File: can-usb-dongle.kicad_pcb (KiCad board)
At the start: 2 copper layers, 41 parts, among them SW1 SW_PUSH, U1 STM32F302C8T, U2 SN65HVD256, U3 NUF2042XV6, U4 MCP1700, U5 SiP32431, X1 16MHz 10ppm

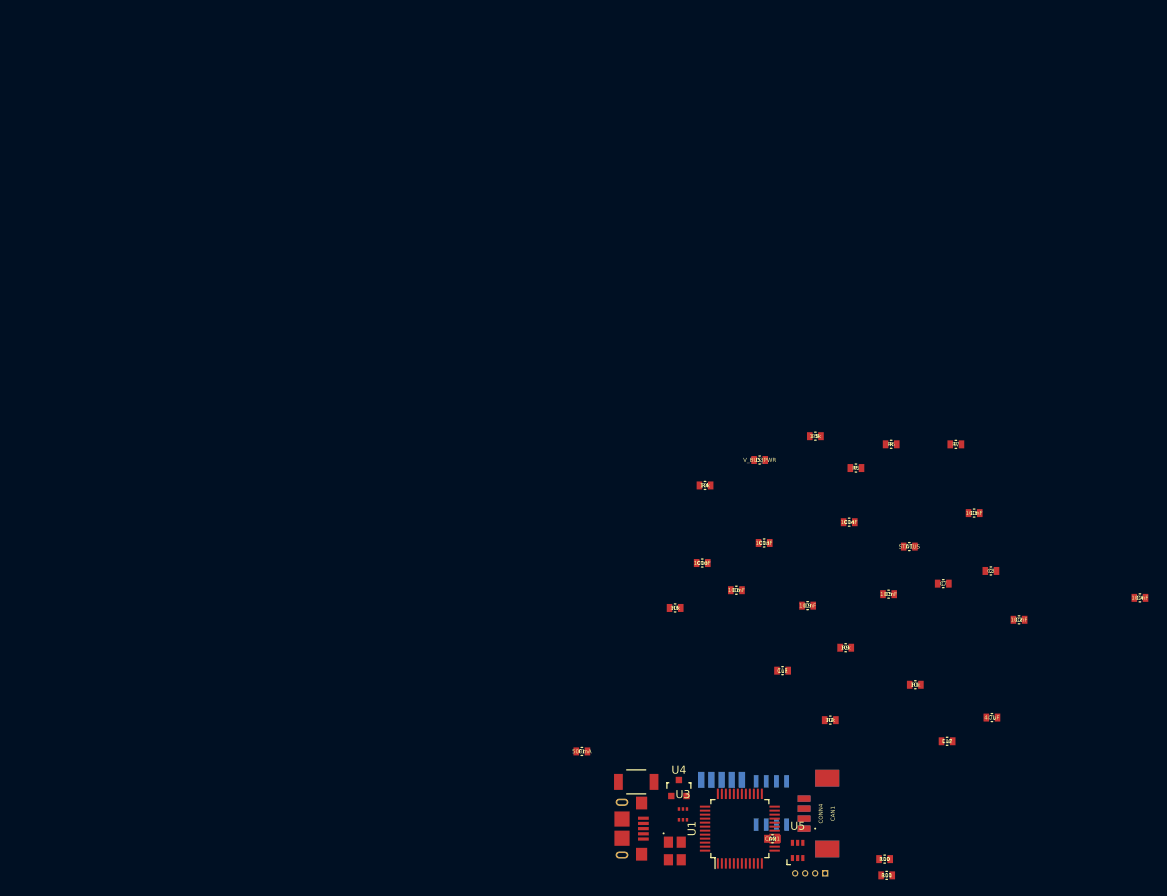
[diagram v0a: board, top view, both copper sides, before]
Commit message: Most components placed.
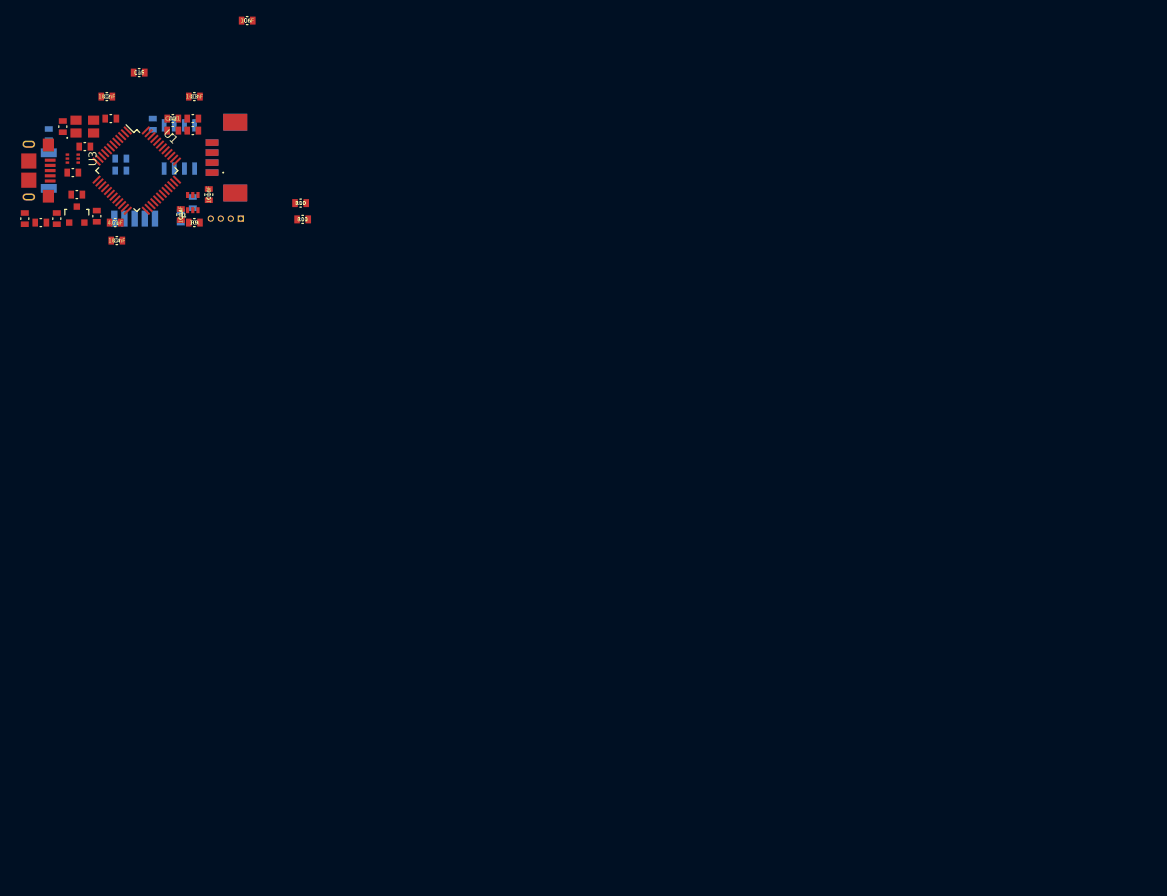
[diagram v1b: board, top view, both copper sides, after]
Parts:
- added C15: 1uF, _std:_0603, F.Cu at (60.3, 32.8)
- C5, C9, R1, R2, R3, R4, SW1: moved to B.Cu
- C6: value 100nF -> 10nF
- C7, C8: value C -> 10pF
- moved C4 135.5 mm to (57.5, 53.8), turned to 180 degrees
- moved C2 131.5 mm to (56.2, 35.8)
- moved C1 125.8 mm to (57.3, 51.5), turned to 180 degrees
- moved C12 124.9 mm to (55.0, 50.7), turned to 90 degrees
- moved C7 124.0 mm to (50.8, 39.5), turned to 270 degrees
- moved C8 123.7 mm to (56.8, 38.5), turned to 180 degrees
- moved R2 122.1 mm to (49.0, 40.5), turned to 90 degrees
- moved R1 118.3 mm to (58.0, 45.0)
- moved D1 117.9 mm to (46.0, 51.0), turned to 90 degrees
- moved D2 117.1 mm to (64.5, 38.5), turned to 180 degrees
- moved X1 116.8 mm to (53.5, 39.5), turned to 0 degrees
- moved U3 112.0 mm to (52.0, 43.5), turned to 90 degrees
- moved U1 111.6 mm to (60.0, 45.0), turned to 315 degrees
- moved U5 110.8 mm to (67.0, 49.0)
- moved CONN3 110.7 mm to (46.5, 45.0)
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
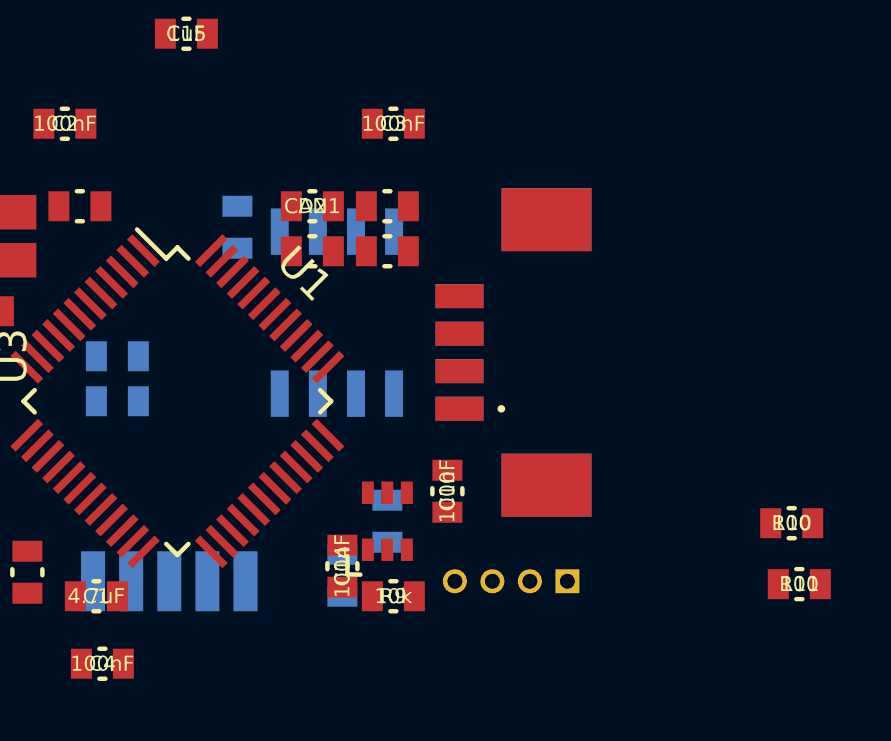
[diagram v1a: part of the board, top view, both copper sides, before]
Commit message: Connect CAN bus power LED to GPIO, update connector footprints.
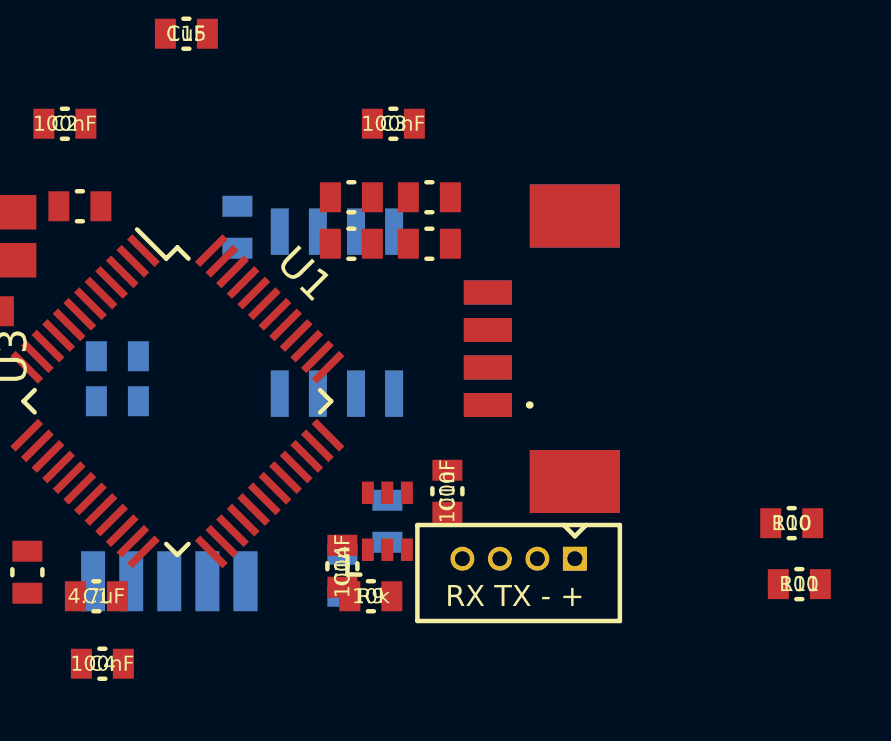
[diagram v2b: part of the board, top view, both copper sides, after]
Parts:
- moved D3 1.43 mm to (68.4, 38.2)
- moved R7 1.42 mm to (68.4, 39.8)
- moved D2 1.33 mm to (65.8, 38.2)
- moved R6 1.32 mm to (65.8, 39.8)
- moved CONN4 0.95 mm to (73.2, 43.2)
- moved CONN5 0.95 mm to (73.2, 43.2)
- moved CONN1 0.79 mm to (73.2, 50.2)
- moved R9 0.75 mm to (66.5, 51.5)
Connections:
- net /CAN1_LED renamed /CAN1_STATUS_LED
- D3 pad 2: /V_BUS -> /CAN1_PWR_LED
- U1 pad 12: Net-(U1-Pad12) -> (no net)
- U1 pad 13: Net-(U1-Pad13) -> (no net)
- U1 pad 14: Net-(U1-Pad14) -> (no net)
- U1 pad 15: Net-(U1-Pad15) -> (no net)
- U1 pad 16: Net-(U1-Pad16) -> (no net)
- U1 pad 17: Net-(U1-Pad17) -> (no net)
- U1 pad 2: Net-(U1-Pad2) -> (no net)
- U1 pad 20: /V_BUS_ENABLE -> /CAN1_PWR_LED
- U1 pad 22: Net-(U1-Pad22) -> (no net)
- U1 pad 25: Net-(U1-Pad25) -> (no net)
- U1 pad 26: Net-(U1-Pad26) -> (no net)
- U1 pad 27: Net-(U1-Pad27) -> (no net)
- U1 pad 28: Net-(U1-Pad28) -> (no net)
- U1 pad 29: Net-(U1-Pad29) -> (no net)
- U1 pad 3: Net-(U1-Pad3) -> (no net)
- U1 pad 30: Net-(U1-Pad30) -> (no net)
- U1 pad 31: Net-(U1-Pad31) -> (no net)
- U1 pad 38: Net-(U1-Pad38) -> (no net)
- U1 pad 39: Net-(U1-Pad39) -> /V_BUS_ENABLE
- U1 pad 4: Net-(U1-Pad4) -> (no net)
- U1 pad 40: Net-(U1-Pad40) -> (no net)
- U1 pad 41: Net-(U1-Pad41) -> (no net)
- U5 pad 6: Net-(U5-Pad6) -> (no net)
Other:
- board text added: "+ - TX RX"
- board text added: "RX TX - +"

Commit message: Change DRC minimal dimmensions
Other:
- net class Default: trace_width 0.25 -> 0.2; via_dia 0.6 -> 0.8
- net class limit added: clearance 0.1524, trace_width 0.1524, via_dia 0.7, via_drill 0.3
- rule trace_min: 0.2 -> 0.1524
- rule via_min_size: 0.4 -> 0.7
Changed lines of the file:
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@@
     (links 115)
     (no_connects 115)
-    (area 0 0 0 0)
+    (area 25.087299 25.474999 91.421702 60.2)
     (thickness 1.6)
     (drawings 8)
@@
   )
   (setup
-    (last_trace_width 0.25)
+    (last_trace_width 0.2)
+    (user_trace_width 0.1524)
+    (user_trace_width 0.16)
+    (user_trace_width 0.2)
+    (user_trace_width 0.25)
     (trace_clearance 0.2)
     (zone_clearance 0.508)
     (zone_45_only no)
-    (trace_min 0.2)
+    (trace_min 0.1524)
     (segment_width 0.2)
     (edge_width 0.1)
-    (via_size 0.6)
+    (via_size 0.8)
     (via_drill 0.4)
-    (via_min_size 0.4)
+    (via_min_size 0.7)
     (via_min_drill 0.3)
+    (user_via 0.7 0.3)
+    (user_via 0.8 0.4)
+    (user_via 0.9 0.4)
+    (user_via 1 0.5)
     (uvia_size 0.3)
     (uvia_drill 0.1)
@@
   (net_class Default "This is the default net class."
     (clearance 0.2)
-    (trace_width 0.25)
-    (via_dia 0.6)
+    (trace_width 0.2)
+    (via_dia 0.8)
     (via_drill 0.4)
     (uvia_dia 0.3)
@@
     (add_net VCC)
   )
+  (net_class limit ""
+    (clearance 0.1524)
+    (trace_width 0.1524)
+    (via_dia 0.7)
+    (via_drill 0.3)
+    (uvia_dia 0.3)
+    (uvia_drill 0.1)
+  )
   (module _connectors:_Molex-PicoBlade-SMD-4 (layer F.Cu)

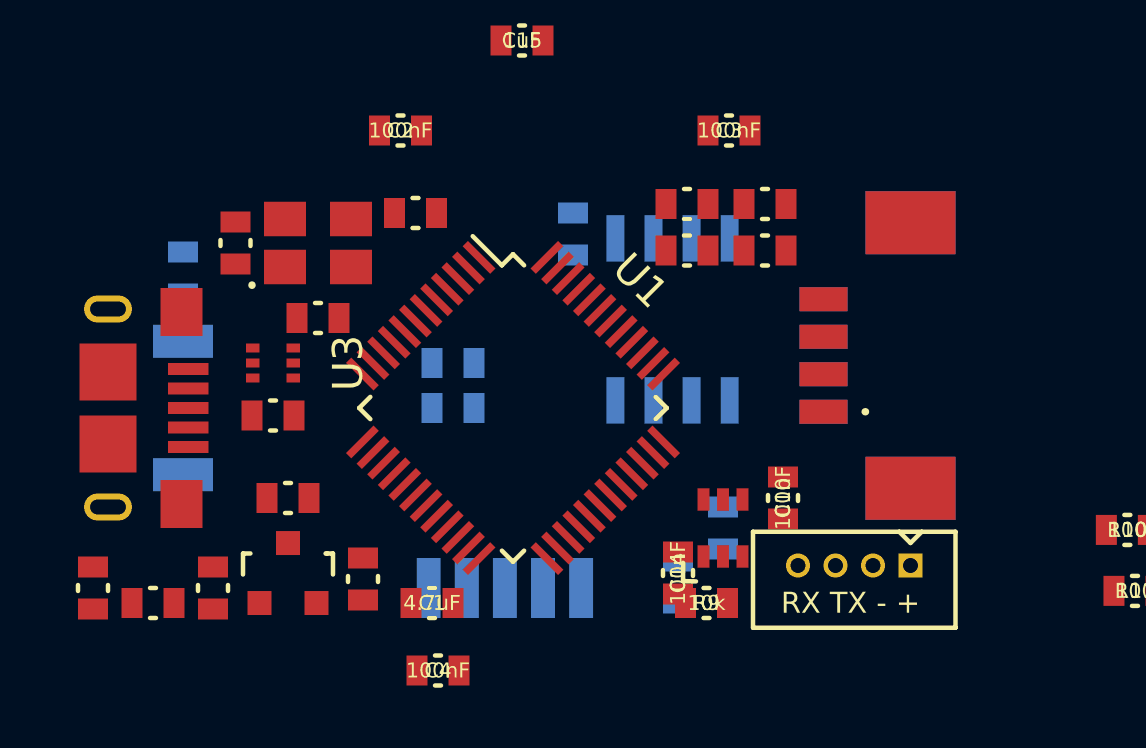
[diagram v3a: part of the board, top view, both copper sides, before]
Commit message: PCB layer setting, correct edge cut layer
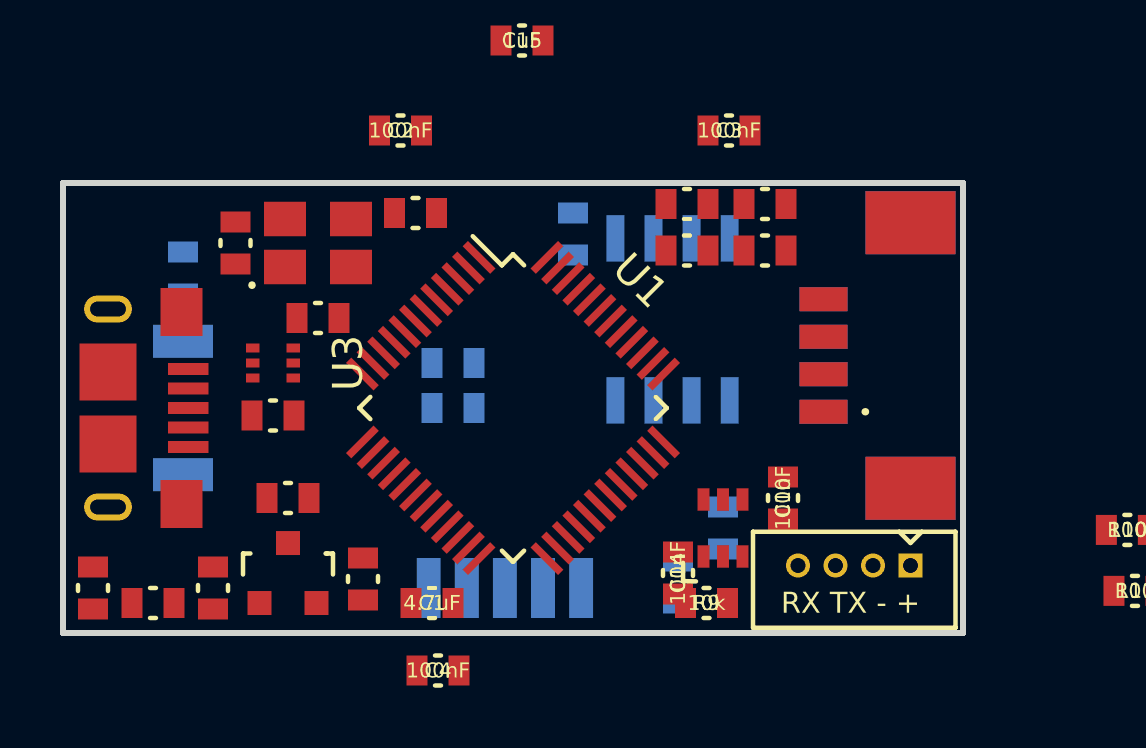
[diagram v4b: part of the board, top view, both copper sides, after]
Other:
- board outline added: 30 x 15 mm
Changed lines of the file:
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@@
     (0 F.Cu signal)
     (31 B.Cu signal)
-    (32 B.Adhes user)
-    (33 F.Adhes user)
     (34 B.Paste user)
     (35 F.Paste user)
@@
     (38 B.Mask user)
     (39 F.Mask user)
-    (40 Dwgs.User user)
     (41 Cmts.User user)
-    (42 Eco1.User user)
-    (43 Eco2.User user)
     (44 Edge.Cuts user)
-    (45 Margin user)
-    (46 B.CrtYd user)
-    (47 F.CrtYd user)
-    (48 B.Fab user)
-    (49 F.Fab user)
   )
   (setup
@@
     (trace_min 0.1524)
     (segment_width 0.2)
-    (edge_width 0.1)
+    (edge_width 0.2)
     (via_size 0.8)
     (via_drill 0.4)
@@
     (arrow2b (pts (xy 45 57.499999) (xy 46.126504 56.913578)))
   )
-  (gr_line (start 75 37.5) (end 45 37.5) (layer Dwgs.User) (width 0.2))
-  (gr_line (start 75 52.5) (end 75 37.5) (layer Dwgs.User) (width 0.2))
-  (gr_line (start 45 52.5) (end 75 52.5) (layer Dwgs.User) (width 0.2))
-  (gr_line (start 45 37.5) (end 45 52.5) (layer Dwgs.User) (width 0.2))
+  (gr_line (start 75 37.5) (end 45 37.5) (layer Edge.Cuts) (width 0.2))
+  (gr_line (start 75 52.5) (end 75 37.5) (layer Edge.Cuts) (width 0.2))
+  (gr_line (start 45 52.5) (end 75 52.5) (layer Edge.Cuts) (width 0.2))
+  (gr_line (start 45 37.5) (end 45 52.5) (layer Edge.Cuts) (width 0.2))
   (segment (start 28.3079 28.8202) (end 28.1174 29.0107) (width 0.25) (layer Dwgs.User) (net 0))
   (segment (start 25.4123 31.7158) (end 28.3079 28.8202) (width 0.25) (layer Dwgs.User) (net 0))

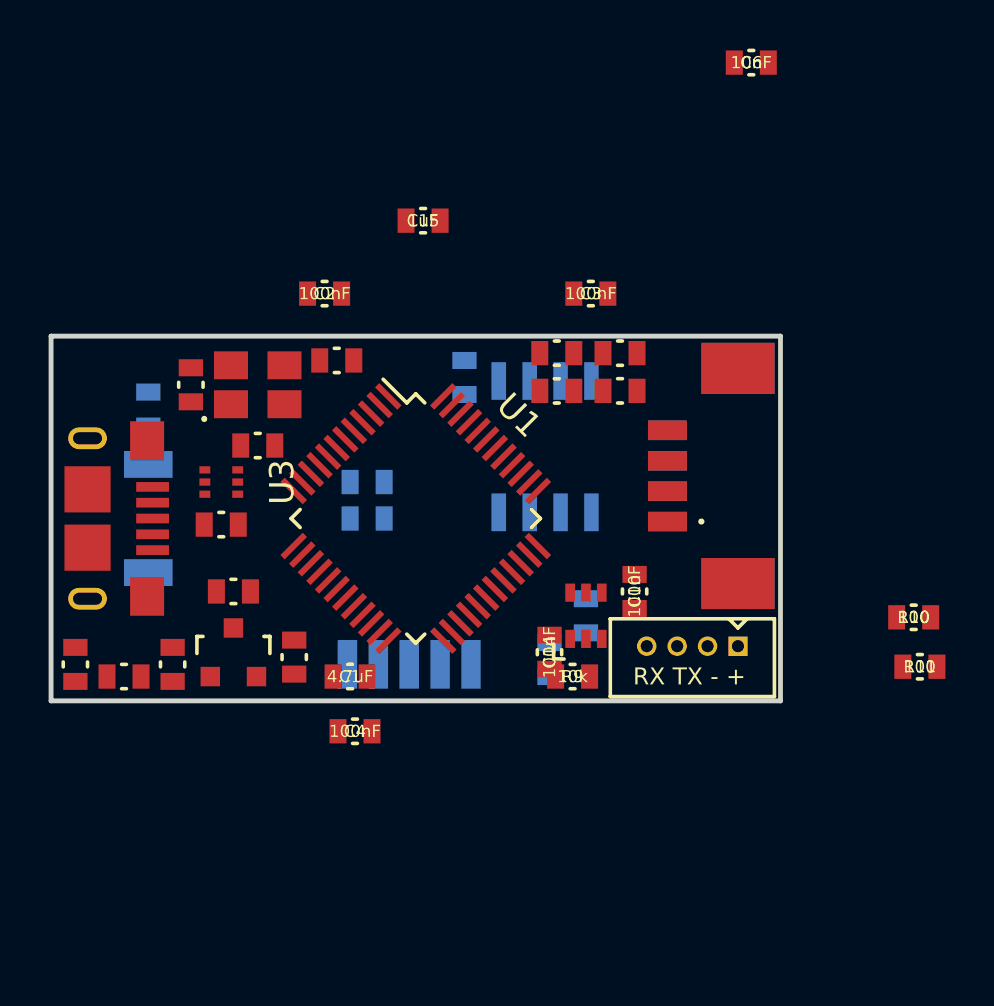
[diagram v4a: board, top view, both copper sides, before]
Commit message: Change pinout to optimize routing.
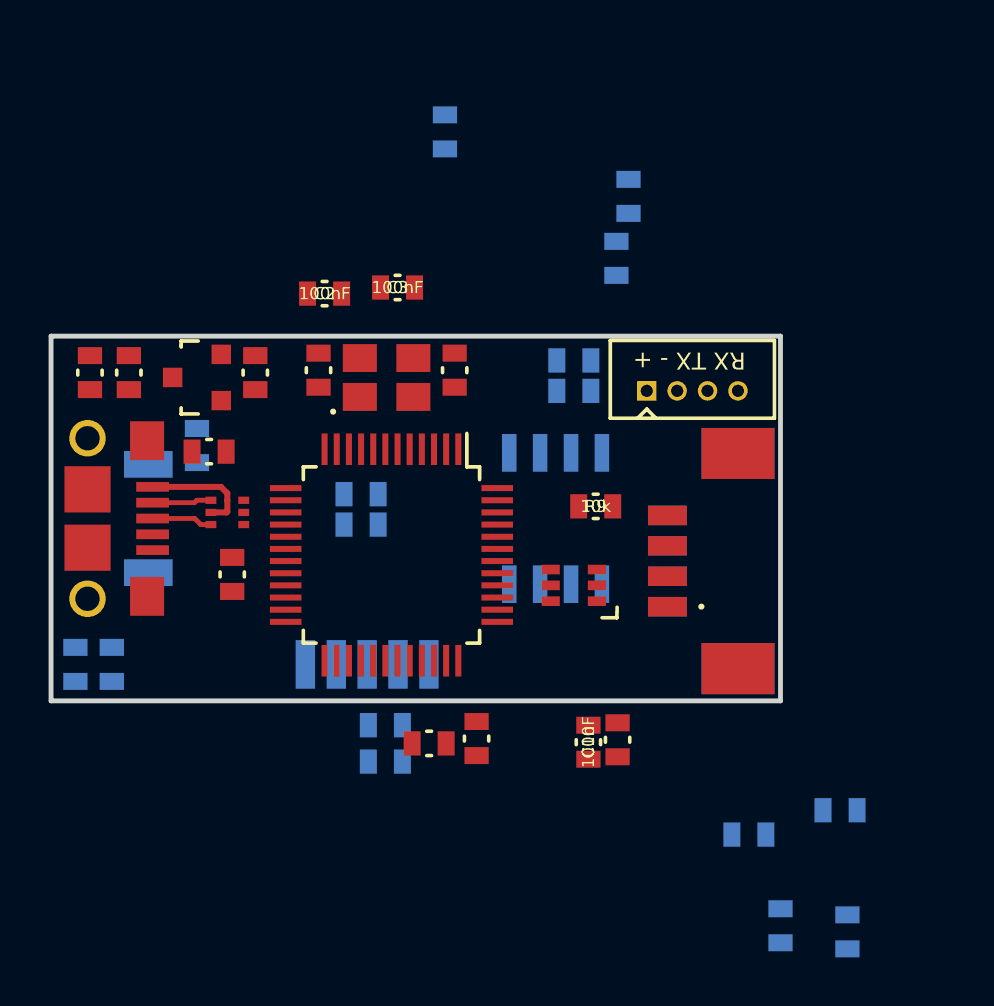
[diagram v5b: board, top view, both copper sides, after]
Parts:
- C15, C6, D1, D2, D3, R10, R11, R5, R6, R7: moved to B.Cu
- CONN3: footprint _connectors:_Micro-USB-AB-receptacle-SMT-th -> _connectors:_Micro-USB-AB-receptacle-SMT-th-no-slot
- moved D2 26.6 mm to (77.8, 62.0), turned to 270 degrees
- moved D3 24.5 mm to (75.0, 61.8), turned to 270 degrees
- moved C6 23.9 mm to (57.8, 44.0)
- moved R6 20.8 mm to (77.5, 57.0), turned to 0 degrees
- moved R7 19.0 mm to (73.7, 58.0)
- moved R11 18.2 mm to (66.5, 39.8), turned to 180 degrees
- moved R10 17.5 mm to (66.5, 38.5), turned to 180 degrees
- moved R3 17.3 mm to (68.8, 31.8)
- moved R4 16.7 mm to (68.2, 34.3)
- moved C15 12.8 mm to (57.8, 45.2)
- moved C11 12.5 mm to (46.6, 39.0)
- moved C12 11.8 mm to (53.4, 39.0), turned to 270 degrees
- moved U4 11.4 mm to (51.0, 39.2), turned to 90 degrees
- moved CONN1 11.1 mm to (69.5, 39.8), turned to 0 degrees
- moved C9 10.1 mm to (61.2, 29.1)
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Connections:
- D1 pad 1: Net-(D1-Pad1) -> GND
- D1 pad 2: /STATUS_LED -> Net-(D1-Pad2)
- D2 pad 1: Net-(D2-Pad1) -> GND
- D2 pad 2: /CAN1_STATUS_LED -> Net-(D2-Pad2)
- D3 pad 1: Net-(D3-Pad1) -> GND
- D3 pad 2: /CAN1_PWR_LED -> Net-(D3-Pad2)
- R5 pad 1: Net-(D1-Pad1) -> /STATUS_LED
- R5 pad 2: GND -> Net-(D1-Pad2)
- R6 pad 1: Net-(D2-Pad1) -> /CAN1_STATUS_LED
- R6 pad 2: GND -> Net-(D2-Pad2)
- R7 pad 1: Net-(D3-Pad1) -> /CAN1_PWR_LED
- R7 pad 2: GND -> Net-(D3-Pad2)
- U1 pad 12: (no net) -> Net-(U1-Pad12)
- U1 pad 13: (no net) -> Net-(U1-Pad13)
- U1 pad 14: (no net) -> Net-(U1-Pad14)
- U1 pad 15: (no net) -> Net-(U1-Pad15)
- U1 pad 16: (no net) -> Net-(U1-Pad16)
- U1 pad 17: (no net) -> Net-(U1-Pad17)
- U1 pad 18: /STATUS_LED -> Net-(U1-Pad18)
- U1 pad 19: /CAN1_STATUS_LED -> Net-(U1-Pad19)
- U1 pad 2: (no net) -> /CAN1_STATUS_LED
- U1 pad 20: /CAN1_PWR_LED -> Net-(U1-Pad20)
- U1 pad 21: /CAN_SILENT -> Net-(U1-Pad21)
- U1 pad 22: (no net) -> Net-(U1-Pad22)
- U1 pad 25: (no net) -> /STATUS_LED
- U1 pad 26: (no net) -> Net-(U1-Pad26)
- U1 pad 27: (no net) -> Net-(U1-Pad27)
- U1 pad 28: (no net) -> Net-(U1-Pad28)
- U1 pad 29: (no net) -> Net-(U1-Pad29)
- U1 pad 3: (no net) -> /CAN1_PWR_LED
- U1 pad 30: (no net) -> Net-(U1-Pad30)
- U1 pad 31: (no net) -> Net-(U1-Pad31)
- U1 pad 38: (no net) -> /V_BUS_ENABLE
- U1 pad 39: /V_BUS_ENABLE -> /CAN_SILENT
- U1 pad 4: (no net) -> Net-(U1-Pad4)
- U1 pad 40: (no net) -> Net-(U1-Pad40)
- U1 pad 41: (no net) -> Net-(U1-Pad41)
- U3 pad 1: /USB_D- -> /USB_D+
- U3 pad 3: /USB_D+ -> /USB_D-
- U3 pad 4: Net-(CONN3-Pad3) -> Net-(CONN3-Pad2)
- U3 pad 6: Net-(CONN3-Pad2) -> Net-(CONN3-Pad3)
- U5 pad 6: (no net) -> Net-(U5-Pad6)
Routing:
- net Net-(C13-Pad1): track 0.00 -> 4.63 mm
- net Net-(CONN3-Pad3): track 0.00 -> 2.50 mm
- net Net-(CONN3-Pad2): track 0.00 -> 2.44 mm
